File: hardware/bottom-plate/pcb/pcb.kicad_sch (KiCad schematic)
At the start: 45 parts, among them U1 Pico

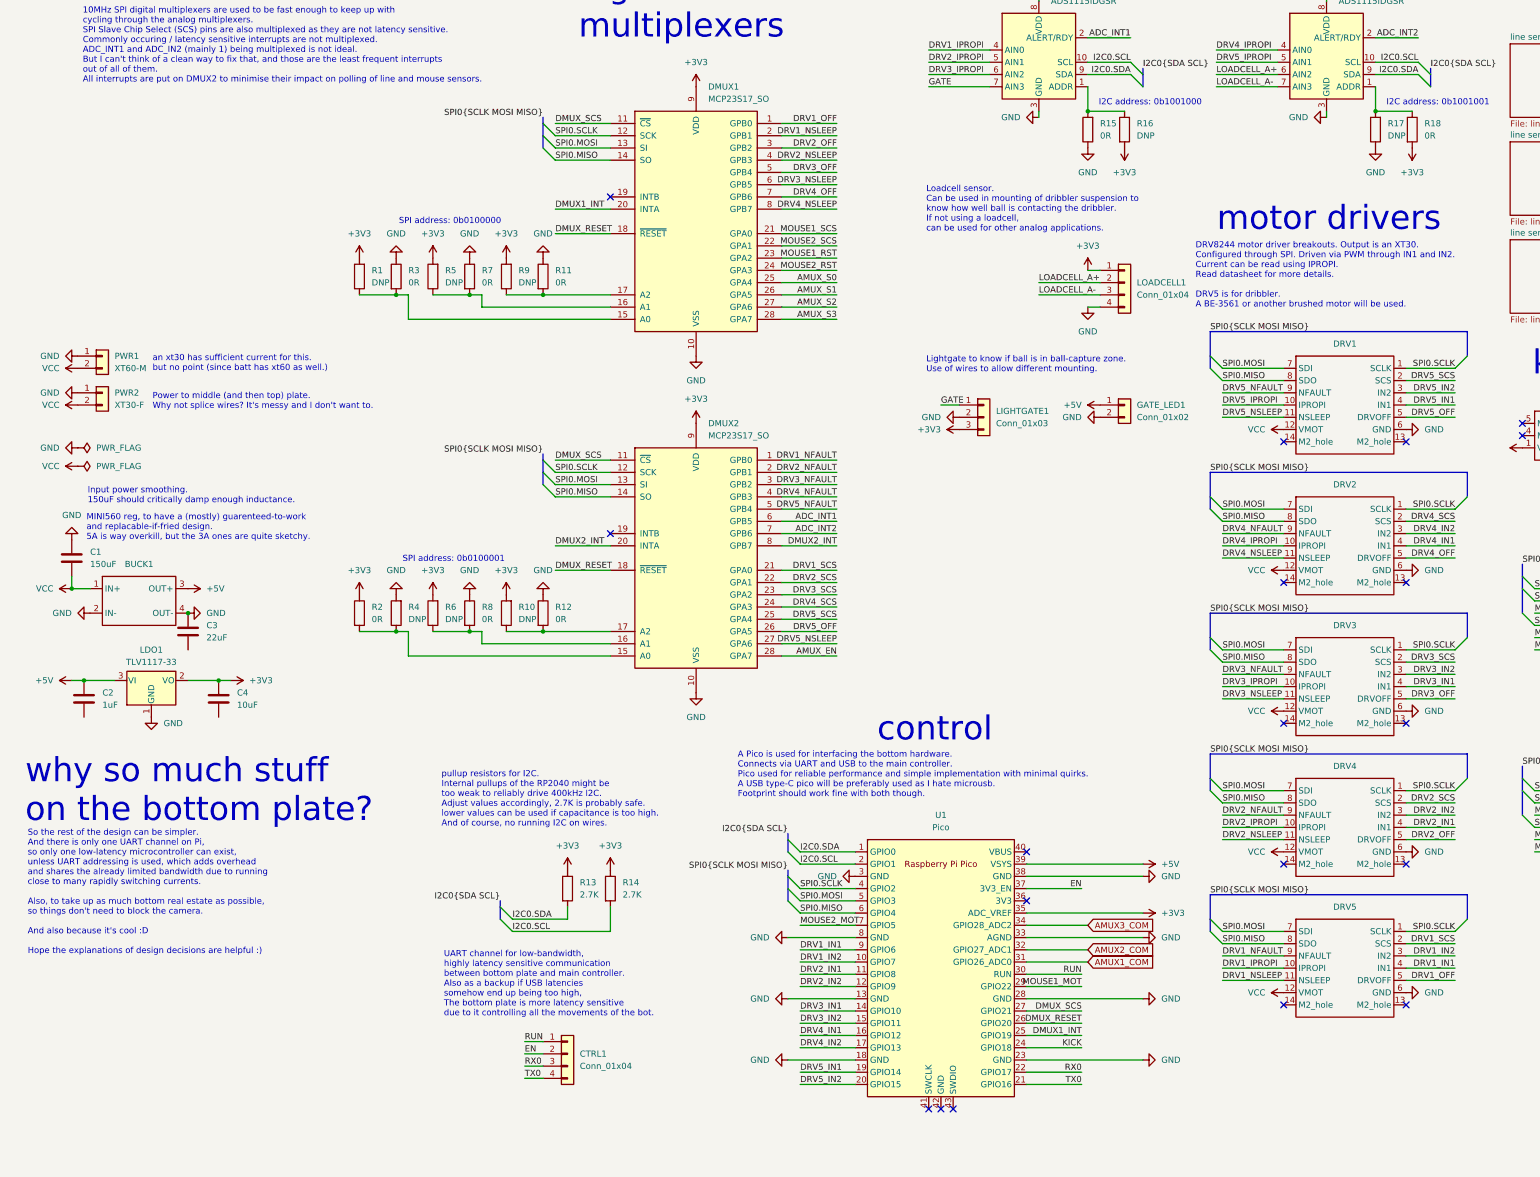
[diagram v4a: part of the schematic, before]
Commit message: fixed non convention following of kicker pcb
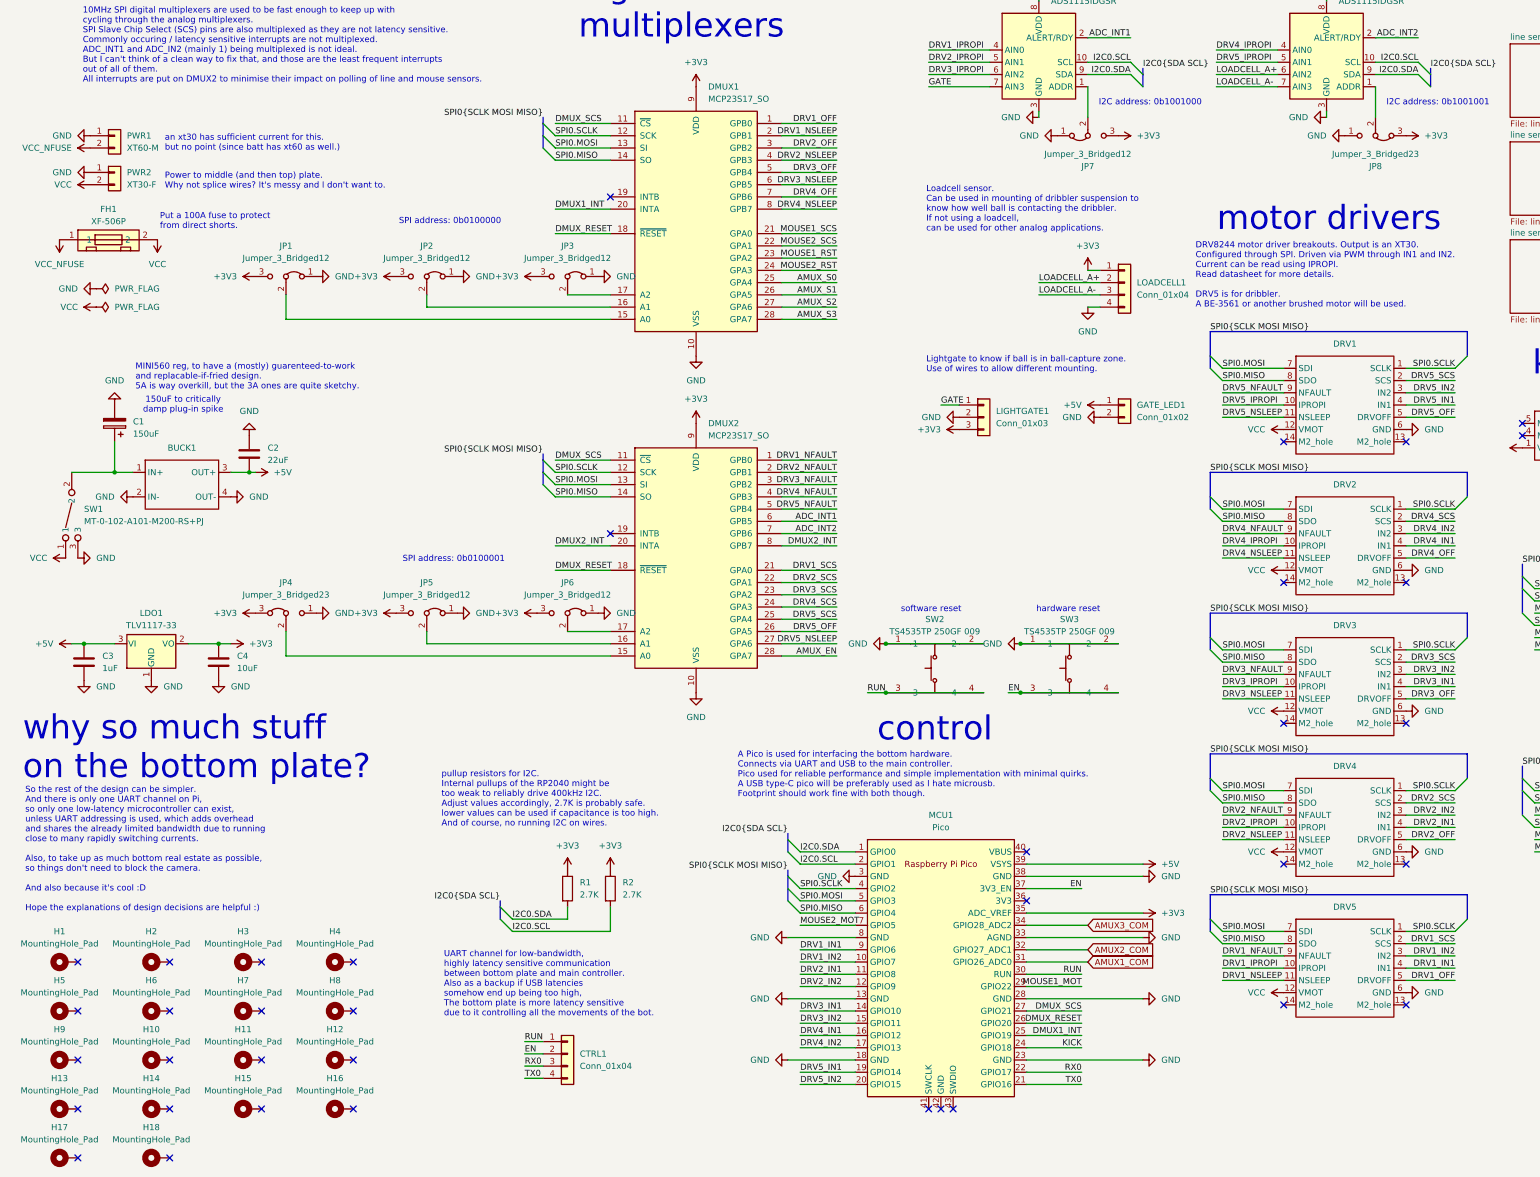
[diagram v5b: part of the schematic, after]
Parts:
- removed C1: 150uF, Capacitor_SMD:CP_Elec_6.3x7.7, symbol Device:C
- removed C3: 22uF, PCM_Capacitor_SMD_AKL:C_0805_2012Metric_Pad1.15x1.40mm_HandSolder, symbol Device:C
- removed R1, R10, R16, R17, R4, R5, R6, R9: DNP, PCM_Resistor_SMD_AKL:R_0805_2012Metric_Pad1.15x1.40mm_HandSolder, symbol Device:R
- removed R11, R12, R15, R18, R2, R3, R7, R8: 0R, PCM_Resistor_SMD_AKL:R_0805_2012Metric_Pad1.15x1.40mm_HandSolder, symbol Device:R
- added C1: 150uF, Capacitor_SMD:CP_Elec_6.3x7.7, symbol Device:C_Polarized
- added C2: 22uF, PCM_Capacitor_SMD_AKL:C_0805_2012Metric_Pad1.15x1.40mm_HandSolder, symbol Device:C
- added FH1: XF-506P, EasyEDA:FUSE-TH_XF-506P, symbol EasyEDA:XF-506P
- added H1, H10, H11, H12, H13, H14, H15, H16, H17, H18, H2, H3, H4, H5, H6, H7, H8, H9: MountingHole_Pad, MountingHole:MountingHole_2.2mm_M2_Pad_Via, symbol Mechanical:MountingHole_Pad
- added JP1, JP2, JP3, JP5, JP6, JP7: Jumper_3_Bridged12, Connector_PinHeader_1.27mm:PinHeader_1x03_P1.27mm_Vertical, symbol Jumper:Jumper_3_Bridged12
- added JP4, JP8: Jumper_3_Bridged23, Connector_PinHeader_1.27mm:PinHeader_1x03_P1.27mm_Vertical, symbol Jumper:Jumper_3_Bridged12
- added SW1: MT-0-102-A101-M200-RS+PJ, EasyEDA:SW-TH_MT-0-103-A101-M200-RS, symbol EasyEDA:MT-0-102-A101-M200-RS+PJ
- added SW2, SW3: TS4535TP 250GF 009, EasyEDA:SW-SMD_4P-L4.5-W4.5-P3.00-LS6.8, symbol EasyEDA:TS4535TP250GF009
- renumbered C2 to C3, U1 to MCU1, R13 to R1, R14 to R2
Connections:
- net +3V3: now also JP1.3 (B), JP2.3 (B), JP3.3 (B), JP4.3 (B), JP5.3 (B), JP6.3 (B), JP7.3 (B), JP8.3 (B)
- net +5V: now also C2.2
- net EN: now also SW3.3, SW3.4
- net GND: now also C3.1, C4.1, C1.2, C2.1, JP1.1 (A), JP2.1 (A), JP3.1 (A), JP4.1 (A), JP5.1 (A), JP6.1 (A), JP7.1 (A), JP8.1 (A), SW1.3, SW2.1, SW2.2, SW3.1, SW3.2
- net RUN: now also SW2.3, SW2.4
- net VCC: now also FH1.2, SW1.1; no longer BUCK1.1 (IN+), PWR1.2 (Pin_2)
- net at ADC1.1 (ADDR): now also JP7.2 (C)
- net at ADC2.1 (ADDR): now also JP8.2 (C)
- net at DMUX2.17 (A2): now also JP6.2 (C)
- net at DMUX1.15 (A0): now also JP1.2 (C)
- net at DMUX1.16 (A1): now also JP2.2 (C)
- net at DMUX1.17 (A2): now also JP3.2 (C)
- net at DMUX2.16 (A1): now also JP5.2 (C)
- net at DMUX2.15 (A0): now also JP4.2 (C)
- new net: BUCK1.1 (IN+), C1.1, SW1.2
- new net VCC_NFUSE: FH1.1, PWR1.2 (Pin_2)
- no-connect marks 33 -> 51
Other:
- note added: "150uF to critically damp plug-in spike"
- note added: "Put a 100A fuse to protect from direct shorts."
- note added: "hardware reset"
- note added: "software reset"
- note removed: "Input power smoothing. 150uF should critically damp enough inductance."
- moved on the sheet: BUCK1, C3, C4, LDO1, PWR1, PWR2

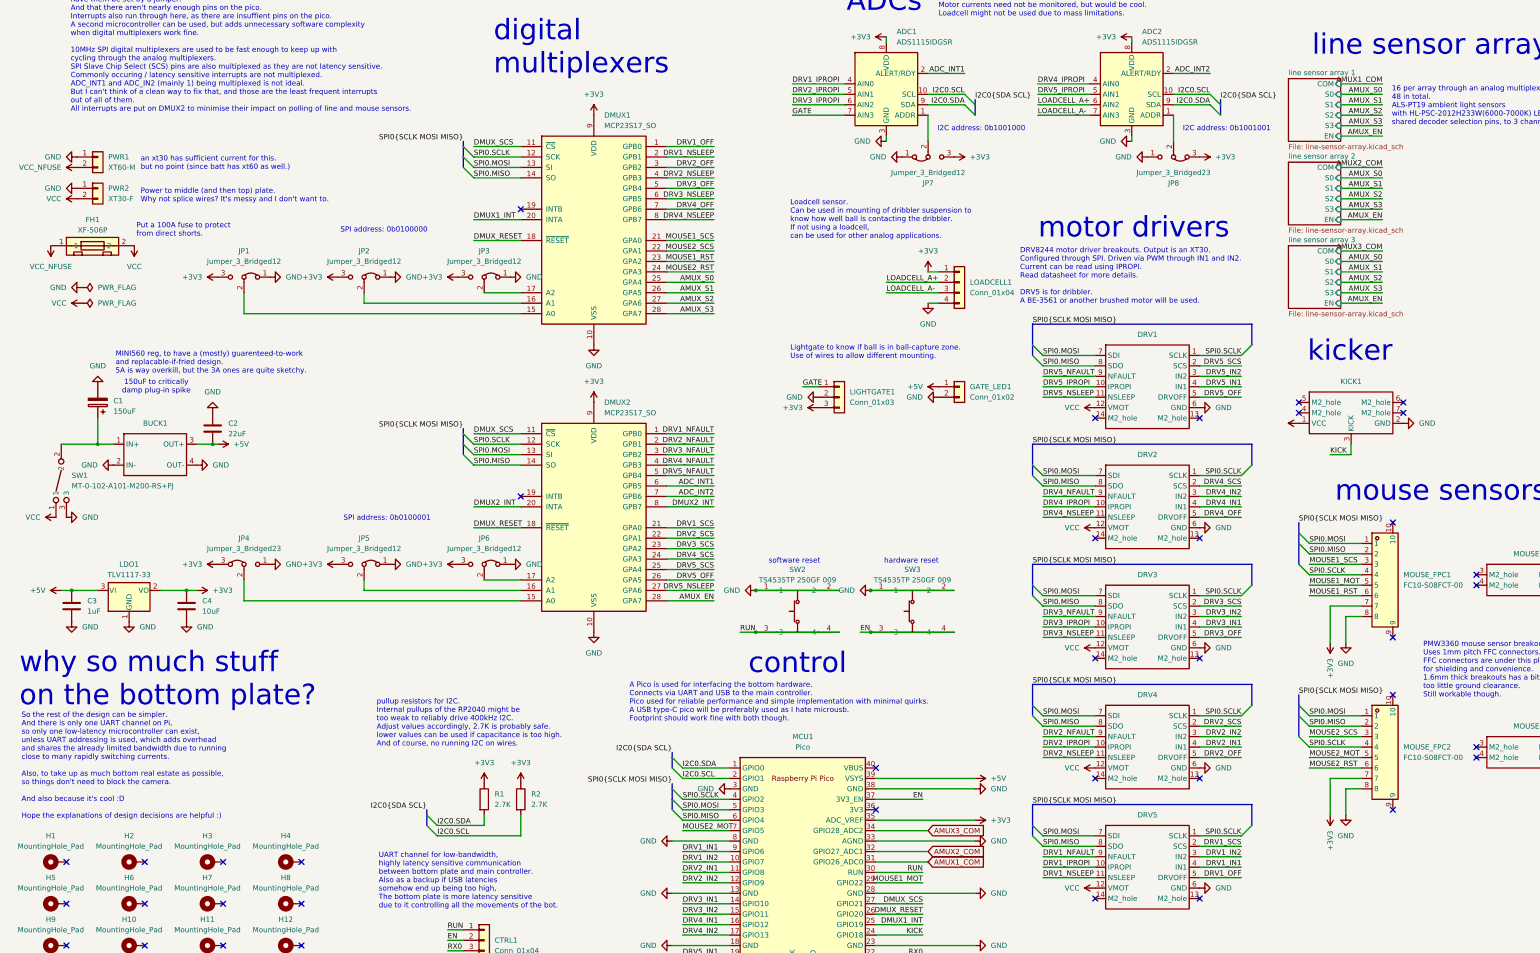
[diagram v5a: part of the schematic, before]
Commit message: fixed line sensor positions
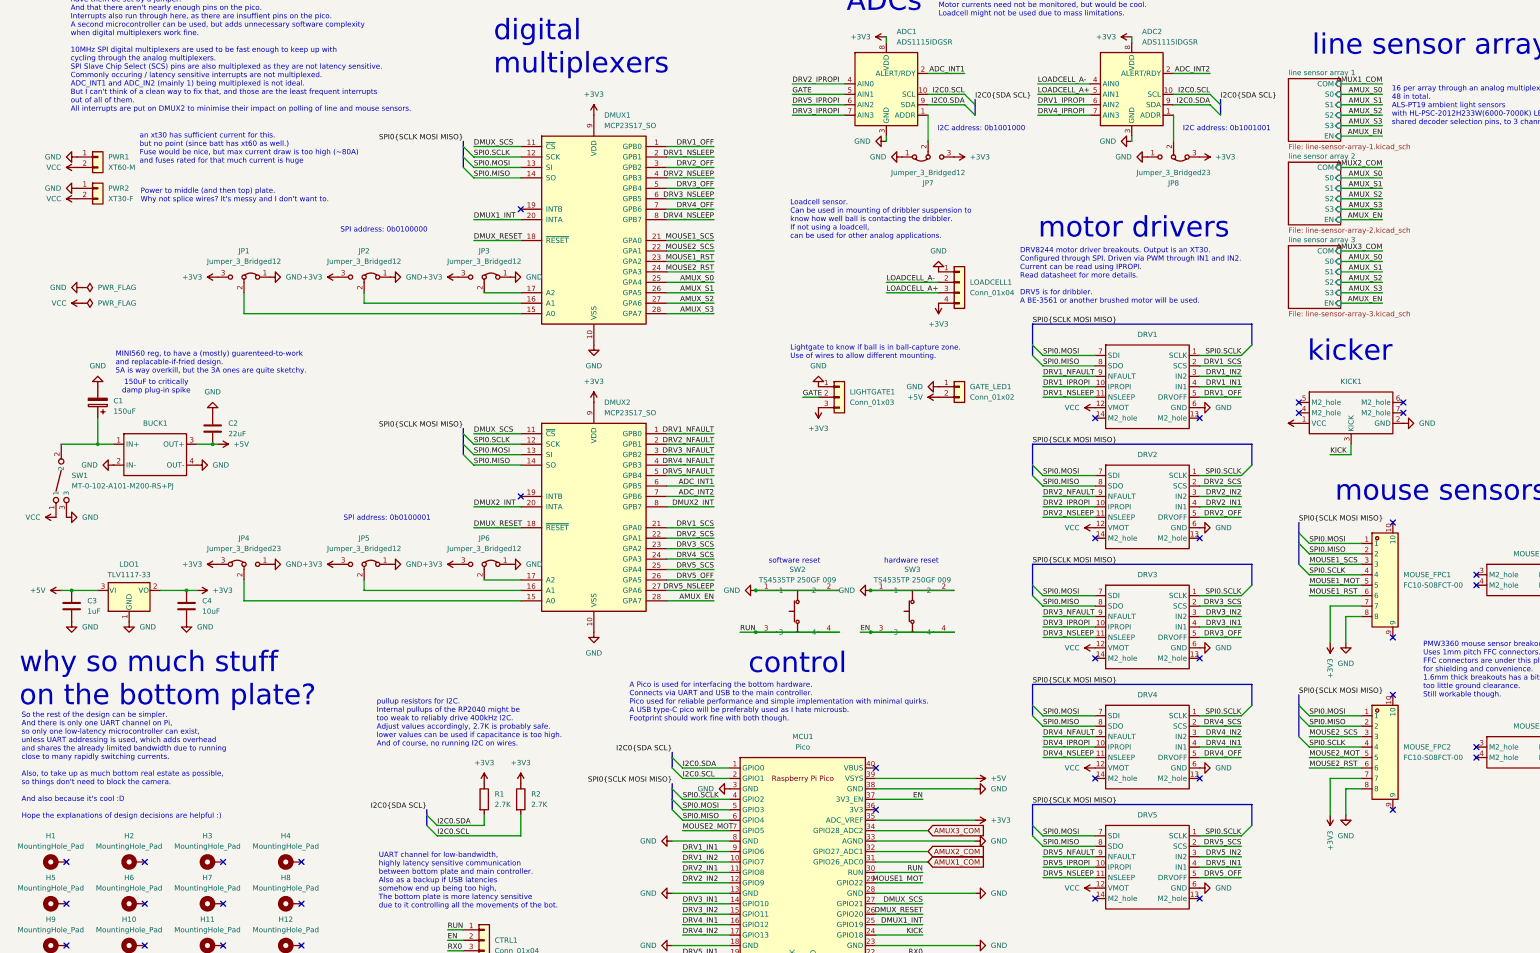
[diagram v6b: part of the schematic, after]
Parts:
- removed FH1: XF-506P, EasyEDA:FUSE-TH_XF-506P, symbol EasyEDA:XF-506P
- H1, H2, H3, H4, H5, H6, H7, H8: footprint MountingHole:MountingHole_2.2mm_M2_Pad_Via -> MountingHole:MountingHole_3.2mm_M3_Pad_Via
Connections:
- net VCC_NFUSE is gone; now on net VCC: PWR1.2 (Pin_2)
- net +3V3: now also LOADCELL1.4 (Pin_4); no longer LOADCELL1.1 (Pin_1)
- net +5V: now also GATE_LED1.2 (Pin_2); no longer GATE_LED1.1 (Pin_1)
- net DRV1_IN1: now also DRV1.4 (IN1); no longer DRV5.4 (IN1)
- net DRV1_IN2: now also DRV1.3 (IN2); no longer DRV5.3 (IN2)
- net DRV1_IPROPI: now also ADC2.6 (AIN2), DRV1.10 (IPROPI); no longer ADC1.4 (AIN0), DRV5.10 (IPROPI)
- net DRV1_NFAULT: now also DRV1.9 (NFAULT); no longer DRV5.9 (NFAULT)
- net DRV1_NSLEEP: now also DRV1.11 (NSLEEP); no longer DRV5.11 (NSLEEP)
- net DRV1_OFF: now also DRV1.5 (DRVOFF); no longer DRV5.5 (DRVOFF)
- net DRV1_SCS: now also DRV1.2 (SCS); no longer DRV5.2 (SCS)
- net DRV2_IN1: now also DRV2.4 (IN1); no longer DRV4.4 (IN1)
- net DRV2_IN2: now also DRV2.3 (IN2); no longer DRV4.3 (IN2)
- net DRV2_IPROPI: now also ADC1.4 (AIN0), DRV2.10 (IPROPI); no longer ADC1.5 (AIN1), DRV4.10 (IPROPI)
- net DRV2_NFAULT: now also DRV2.9 (NFAULT); no longer DRV4.9 (NFAULT)
- net DRV2_NSLEEP: now also DRV2.11 (NSLEEP); no longer DRV4.11 (NSLEEP)
- net DRV2_OFF: now also DRV2.5 (DRVOFF); no longer DRV4.5 (DRVOFF)
- net DRV2_SCS: now also DRV2.2 (SCS); no longer DRV4.2 (SCS)
- net DRV3_IPROPI: now also ADC1.7 (AIN3); no longer ADC1.6 (AIN2)
- net DRV4_IN1: now also DRV4.4 (IN1); no longer DRV2.4 (IN1)
- net DRV4_IN2: now also DRV4.3 (IN2); no longer DRV2.3 (IN2)
- net DRV4_IPROPI: now also ADC2.7 (AIN3), DRV4.10 (IPROPI); no longer ADC2.4 (AIN0), DRV2.10 (IPROPI)
- net DRV4_NFAULT: now also DRV4.9 (NFAULT); no longer DRV2.9 (NFAULT)
- net DRV4_NSLEEP: now also DRV4.11 (NSLEEP); no longer DRV2.11 (NSLEEP)
- net DRV4_OFF: now also DRV4.5 (DRVOFF); no longer DRV2.5 (DRVOFF)
- net DRV4_SCS: now also DRV4.2 (SCS); no longer DRV2.2 (SCS)
- net DRV5_IN1: now also DRV5.4 (IN1); no longer DRV1.4 (IN1)
- net DRV5_IN2: now also DRV5.3 (IN2); no longer DRV1.3 (IN2)
- net DRV5_IPROPI: now also ADC1.6 (AIN2), DRV5.10 (IPROPI); no longer ADC2.5 (AIN1), DRV1.10 (IPROPI)
- net DRV5_NFAULT: now also DRV5.9 (NFAULT); no longer DRV1.9 (NFAULT)
- net DRV5_NSLEEP: now also DRV5.11 (NSLEEP); no longer DRV1.11 (NSLEEP)
- net DRV5_OFF: now also DRV5.5 (DRVOFF); no longer DRV1.5 (DRVOFF)
- net DRV5_SCS: now also DRV5.2 (SCS); no longer DRV1.2 (SCS)
- net GATE: now also ADC1.5 (AIN1), LIGHTGATE1.2 (Pin_2); no longer ADC1.7 (AIN3), LIGHTGATE1.1 (Pin_1)
- net GND: now also GATE_LED1.1 (Pin_1), LIGHTGATE1.1 (Pin_1), LOADCELL1.1 (Pin_1); no longer GATE_LED1.2 (Pin_2), LIGHTGATE1.2 (Pin_2), LOADCELL1.4 (Pin_4)
- net LOADCELL_A+: now also ADC2.5 (AIN1), LOADCELL1.3 (Pin_3); no longer ADC2.6 (AIN2), LOADCELL1.2 (Pin_2)
- net LOADCELL_A-: now also ADC2.4 (AIN0), LOADCELL1.2 (Pin_2); no longer ADC2.7 (AIN3), LOADCELL1.3 (Pin_3)
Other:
- sheet line sensor array 1: file line-sensor-array.kicad_sch -> line-sensor-array-1.kicad_sch
- sheet line sensor array 2: file line-sensor-array.kicad_sch -> line-sensor-array-2.kicad_sch
- sheet line sensor array 3: file line-sensor-array.kicad_sch -> line-sensor-array-3.kicad_sch
- note added: "an xt30 has sufficient current for this. but no point (since batt has xt60 as well.) Fuse would be nice, but max current draw is too high (~80A) and fuses rated for that much current is huge"
- note removed: "Put a 100A fuse to protect from direct shorts."
- note removed: "an xt30 has sufficient current for this. but no point (since batt has xt60 as well.)"
